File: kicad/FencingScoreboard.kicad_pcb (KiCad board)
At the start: 2 copper layers, 134.5 x 61 mm, 17 parts, among them IC1 PIC16F18855-I-ML, IC2 TLC59281RGE, IC3 TLC59281RGE, J1 USB_B_Micro, J2 Conn_01x04_Socket, Q1 2N7002

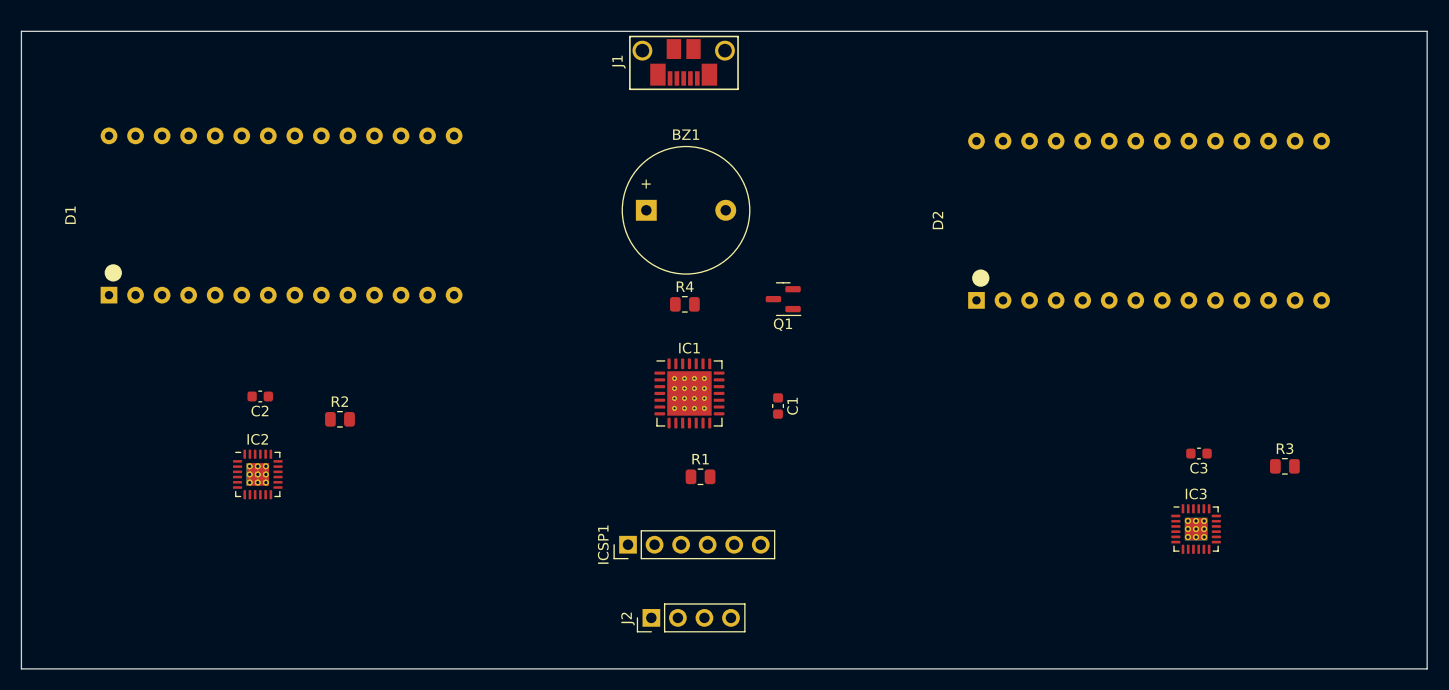
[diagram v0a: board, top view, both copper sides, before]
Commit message: Redesign for new LED driver, route PCB
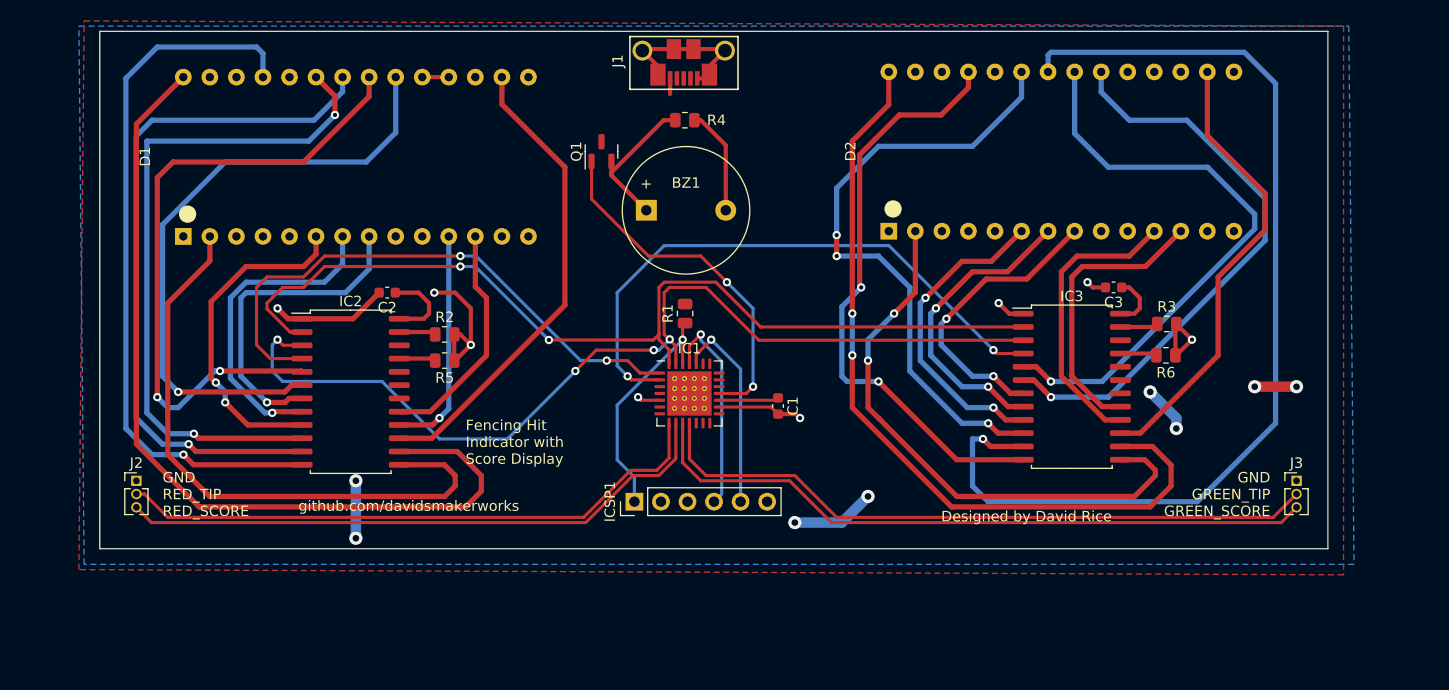
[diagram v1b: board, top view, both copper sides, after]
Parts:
- added J3: Conn_01x03_Pin, Connector_PinHeader_1.27mm:PinHeader_1x03_P1.27mm_Vertical, F.Cu at (204.0, 116.5)
- added R5: 10K, Resistor_SMD:R_0805_2012Metric, F.Cu at (122.5, 105.0)
- added R6: 10K, Resistor_SMD:R_0805_2012Metric, F.Cu at (191.5, 104.5)
- IC2, IC3: value TLC59281RGE -> STP16CPC26; footprint Package_DFN_QFN:QFN-24-1EP_4x4mm_P0.5mm_EP2.15x2.15mm_ThermalVias -> Package_SO:SOP-24_7.5x15.4mm_P1.27mm
- J2: value Conn_01x04_Socket -> Conn_01x03_Pin; footprint Connector_PinHeader_2.54mm:PinHeader_1x04_P2.54mm_Vertical -> Connector_PinHeader_1.27mm:PinHeader_1x03_P1.27mm_Vertical
- R2, R3: value 3K6 -> 2K
- moved J2 51.0 mm to (93.0, 116.5), turned to 0 degrees
- moved Q1 22.4 mm to (137.5, 85.0), turned to 90 degrees
- moved IC3 18.1 mm to (182.5, 107.5)
- moved C3 17.9 mm to (186.5, 98.0)
- moved R3 17.7 mm to (191.6, 101.5)
- moved R4 17.6 mm to (145.5, 82.0), turned to 180 degrees
- moved C2 15.7 mm to (117.0, 98.5)
- moved R1 15.7 mm to (145.5, 100.5), turned to 90 degrees
- moved R2 12.9 mm to (122.5, 102.5)
- moved IC2 11.9 mm to (113.5, 108.0)
- moved D2 10.7 mm to (165.0, 92.6)
- moved D1 9.06 mm to (97.5, 93.1)
- moved ICSP1 4.16 mm to (140.7, 118.5)
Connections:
- net Net-(IC1-ICSPCLK/RB6) renamed ICSPCLK
- net Net-(IC1-ISCPDAT/RB7) renamed ICSPDAT
- net Net-(IC1-RE3/~{MCLR}/VPP) renamed ~{MCLR}
- IC1 pad 10: Net-(IC1-RC2) -> GSC
- IC1 pad 11: Net-(IC1-RC3) -> GTIP
- IC1 pad 8: Net-(IC1-RC0) -> RTIP
- IC1 pad 9: Net-(IC1-RC1) -> RSC
- IC2 pad 1: Net-(IC1-RA2) -> GND
- IC2 pad 10: Net-(D1-D1D-) -> Net-(D1-D2F-)
- IC2 pad 11: Net-(D1-D1G-) -> Net-(D1-D2G-)
- IC2 pad 12: Net-(D1-D3A-) -> Net-(D1-D1A-)
- IC2 pad 13: Net-(D1-D3D-) -> Net-(D1-D1D-)
- IC2 pad 14: Net-(D1-D3G-) -> Net-(D1-D1G-)
- IC2 pad 15: unconnected-(IC2-OUT13-Pad15) -> Net-(D1-D3A-)
- IC2 pad 16: unconnected-(IC2-OUT14-Pad16) -> Net-(D1-D3D-)
- IC2 pad 17: unconnected-(IC2-OUT15-Pad17) -> Net-(D1-D3G-)
- IC2 pad 2: Net-(D1-D2A-) -> Net-(IC1-RA1)
- IC2 pad 20: Net-(IC2-IREF) -> unconnected-(IC2-OUT15-Pad20)
- IC2 pad 21: +5V -> Net-(IC2-~{OE})
- IC2 pad 22: GND -> unconnected-(IC2-SDO-Pad22)
- IC2 pad 23: Net-(IC1-RA1) -> Net-(IC2-R-EXT)
- IC2 pad 24: Net-(IC1-RA0) -> +5V
- IC2 pad 3: Net-(D1-D2B-) -> Net-(IC1-RA0)
- IC2 pad 4: Net-(D1-D2C-) -> Net-(IC1-RA2)
- IC2 pad 5: Net-(D1-D2D-) -> Net-(D1-D2A-)
- IC2 pad 6: Net-(D1-D2E-) -> Net-(D1-D2B-)
- IC2 pad 7: Net-(D1-D2F-) -> Net-(D1-D2C-)
- IC2 pad 8: Net-(D1-D2G-) -> Net-(D1-D2D-)
- IC2 pad 9: Net-(D1-D1A-) -> Net-(D1-D2E-)
- IC3 pad 1: Net-(IC1-RA3) -> GND
- IC3 pad 10: Net-(D2-D1D-) -> Net-(D2-D2F-)
- IC3 pad 11: Net-(D2-D1G-) -> Net-(D2-D2G-)
- IC3 pad 12: Net-(D2-D3A-) -> Net-(D2-D1A-)
- IC3 pad 13: Net-(D2-D3D-) -> Net-(D2-D1D-)
- IC3 pad 14: Net-(D2-D3G-) -> Net-(D2-D1G-)
- IC3 pad 15: unconnected-(IC3-OUT13-Pad15) -> Net-(D2-D3A-)
- IC3 pad 16: unconnected-(IC3-OUT14-Pad16) -> Net-(D2-D3D-)
- IC3 pad 17: unconnected-(IC3-OUT15-Pad17) -> Net-(D2-D3G-)
- IC3 pad 2: Net-(D2-D2A-) -> Net-(IC1-RA1)
- IC3 pad 20: Net-(IC3-IREF) -> unconnected-(IC3-OUT15-Pad20)
- IC3 pad 21: +5V -> Net-(IC3-~{OE})
- IC3 pad 22: GND -> unconnected-(IC3-SDO-Pad22)
- IC3 pad 23: Net-(IC1-RA1) -> Net-(IC3-R-EXT)
- IC3 pad 24: Net-(IC1-RA0) -> +5V
- IC3 pad 3: Net-(D2-D2B-) -> Net-(IC1-RA0)
- IC3 pad 4: Net-(D2-D2C-) -> Net-(IC1-RA3)
- IC3 pad 5: Net-(D2-D2D-) -> Net-(D2-D2A-)
- IC3 pad 6: Net-(D2-D2E-) -> Net-(D2-D2B-)
- IC3 pad 7: Net-(D2-D2F-) -> Net-(D2-D2C-)
- IC3 pad 8: Net-(D2-D2G-) -> Net-(D2-D2D-)
- IC3 pad 9: Net-(D2-D1A-) -> Net-(D2-D2E-)
- J2 pad 1: Net-(IC1-RC0) -> GND
- J2 pad 2: Net-(IC1-RC1) -> RTIP
- J2 pad 3: Net-(IC1-RC2) -> RSC
- R2 pad 1: Net-(IC2-IREF) -> Net-(IC2-R-EXT)
- R3 pad 1: Net-(IC3-IREF) -> Net-(IC3-R-EXT)
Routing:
- net Net-(D2-D2G-): track 0.00 -> 99.6 mm, vias 0 -> 1
- net Net-(IC1-RA0): track 0.00 -> 94.4 mm, vias 0 -> 4
- net Net-(IC1-RA1): track 0.00 -> 91.4 mm, vias 0 -> 2
- net Net-(D1-D1G-): track 0.00 -> 83.4 mm
- net GND: track 0.00 -> 77.3 mm, vias 0 -> 10
- net Net-(D2-D1G-): track 0.00 -> 76.4 mm, vias 0 -> 2
- net Net-(D1-D1A-): track 0.00 -> 68.7 mm, vias 0 -> 1
- net Net-(D1-D2G-): track 0.00 -> 67.0 mm, vias 0 -> 1
- net GSC: track 0.00 -> 65.5 mm
- net Net-(D1-D2F-): track 0.00 -> 65.3 mm, vias 0 -> 2
- net GTIP: track 0.00 -> 64.8 mm
- net Net-(D1-D2A-): track 0.00 -> 62.1 mm, vias 0 -> 2
- net Net-(D1-D2B-): track 0.00 -> 60.0 mm, vias 0 -> 1
- net Net-(D2-D2F-): track 0.00 -> 59.8 mm, vias 0 -> 3
- net Net-(D1-D1D-): track 0.00 -> 58.9 mm
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- added copper zone on F.Cu, net +5V
- added copper zone on B.Cu, net GND
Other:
- board size 134.5 x 61 mm -> 117.5 x 49.5 mm
- board text added: "Designed by David Rice"
- board text added: "Fencing Hit Indicator with Score Display"
- board text added: "GND GREEN_TIP GREEN_SCORE"
- board text added: "GND RED_TIP RED_SCORE"
- board text added: "github.com/davidsmakerworks"

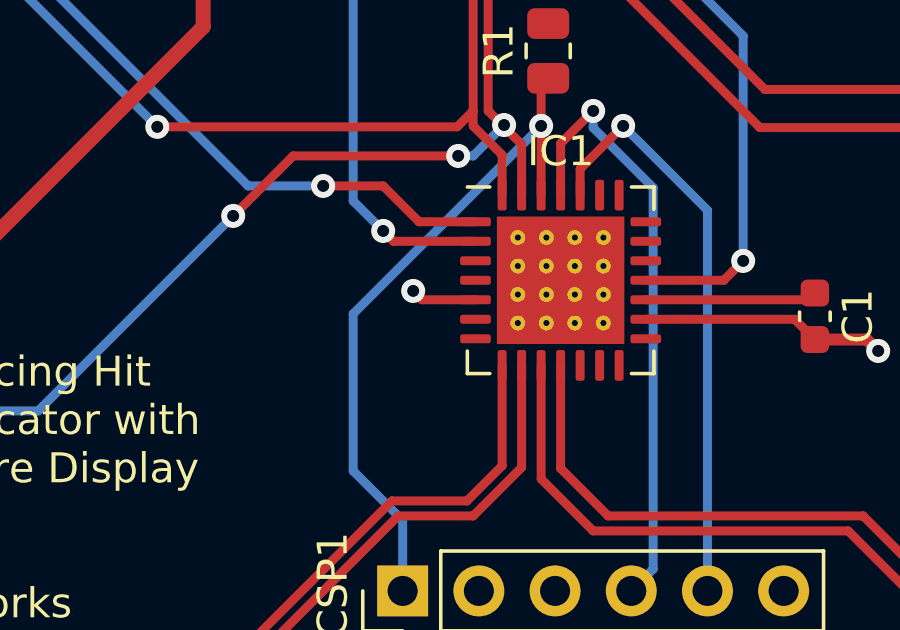
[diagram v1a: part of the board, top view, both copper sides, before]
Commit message: Update design rules, remove thermal vias
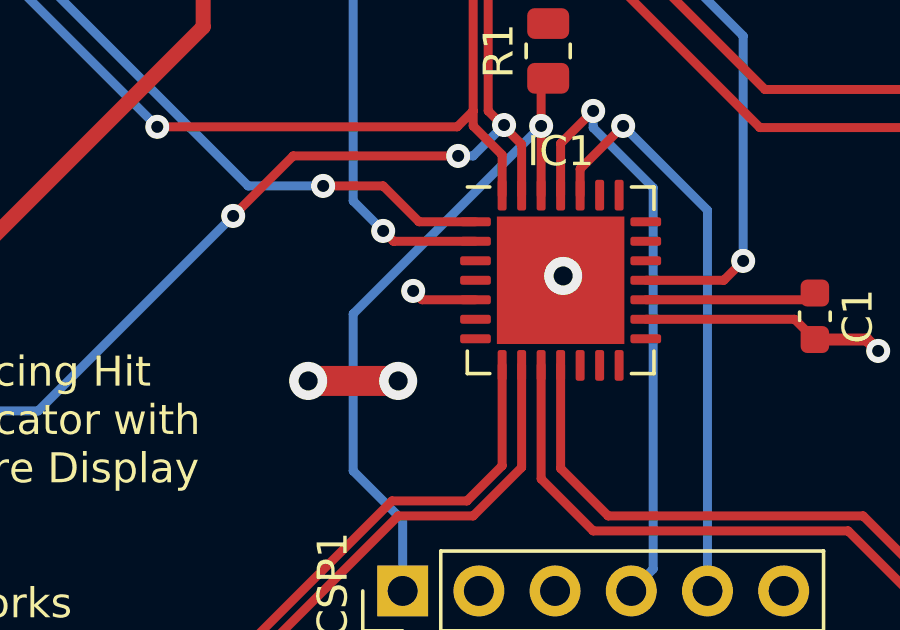
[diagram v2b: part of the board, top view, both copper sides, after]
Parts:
- IC1: footprint Package_DFN_QFN:QFN-28-1EP_6x6mm_P0.65mm_EP4.25x4.25mm_ThermalVias -> Package_DFN_QFN:QFN-28-1EP_6x6mm_P0.65mm_EP4.25x4.25mm
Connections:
- IC1 pad 29: (no net) -> GND
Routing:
- net GND: track 77.3 -> 80.5 mm, vias 10 -> 13

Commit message: Minor updates
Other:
- board text added: "GREEN"
- board text added: "RED"
- board text added: "USB_PWR"
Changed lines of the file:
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@@
     (property "ki_keywords" "cap capacitor")
     (attr smd)
-    (fp_text reference "C2" (at 0 -1.43) (layer "F.SilkS")
+    (fp_text reference "C2" (at 0 1.5) (layer "F.SilkS")
         (effects (font (size 1 1) (thickness 0.15)))
     )
@@
     (property "ki_keywords" "cap capacitor")
     (attr smd)
-    (fp_text reference "C3" (at 0 -1.43) (layer "F.SilkS")
+    (fp_text reference "C3" (at 0 1.5) (layer "F.SilkS")
         (effects (font (size 1 1) (thickness 0.15)))
     )
@@
     (property "ki_keywords" "connector")
     (attr through_hole)
-    (fp_text reference "ICSP1" (at 0 -2.33 90) (layer "F.SilkS")
+    (fp_text reference "ICSP1" (at -3 6.35 180) (layer "F.SilkS")
         (effects (font (size 1 1) (thickness 0.15)))
     )
@@
     (effects (font (size 1 1) (thickness 0.15)) (justify left bottom))
   )
-  (gr_text "Designed by David Rice" (at 170 120.5) (layer "F.SilkS")
+  (gr_text "GREEN" (at 170 88) (layer "F.SilkS")
+    (effects (font (size 5 5) (thickness 0.4)) (justify left bottom))
+  )
+  (gr_text "Designed by David Rice" (at 168 119) (layer "F.SilkS")
     (effects (font (size 1 1) (thickness 0.15)) (justify left bottom))
   )
-  (gr_text "Fencing Hit\nIndicator with\nScore Display" (at 124.5 115) (layer "F.SilkS")
+  (gr_text "RED" (at 106 89) (layer "F.SilkS")
+    (effects (font (size 5 5) (thickness 0.4)) (justify left bottom))
+  )
+  (gr_text "Fencing Hit\nIndicator with\nScore Display" (at 126 113.5) (layer "F.SilkS")
     (effects (font (size 1 1) (thickness 0.15)) (justify left bottom))
   )
-  (gr_text "github.com/davidsmakerworks" (at 108.5 119.5) (layer "F.SilkS")
+  (gr_text "github.com/davidsmakerworks" (at 166 121) (layer "F.SilkS")
     (effects (font (size 1 1) (thickness 0.15)) (justify left bottom))
   )
@@
     (effects (font (size 1 1) (thickness 0.15)) (justify right bottom))
   )
+  (gr_text "USB_PWR" (at 152 76.5) (layer "F.SilkS")
+    (effects (font (size 1 1) (thickness 0.15)) (justify left bottom))
+  )
   (segment (start 138.45 87) (end 138.45 87.28) (width 0.4) (layer "F.Cu") (net 1))

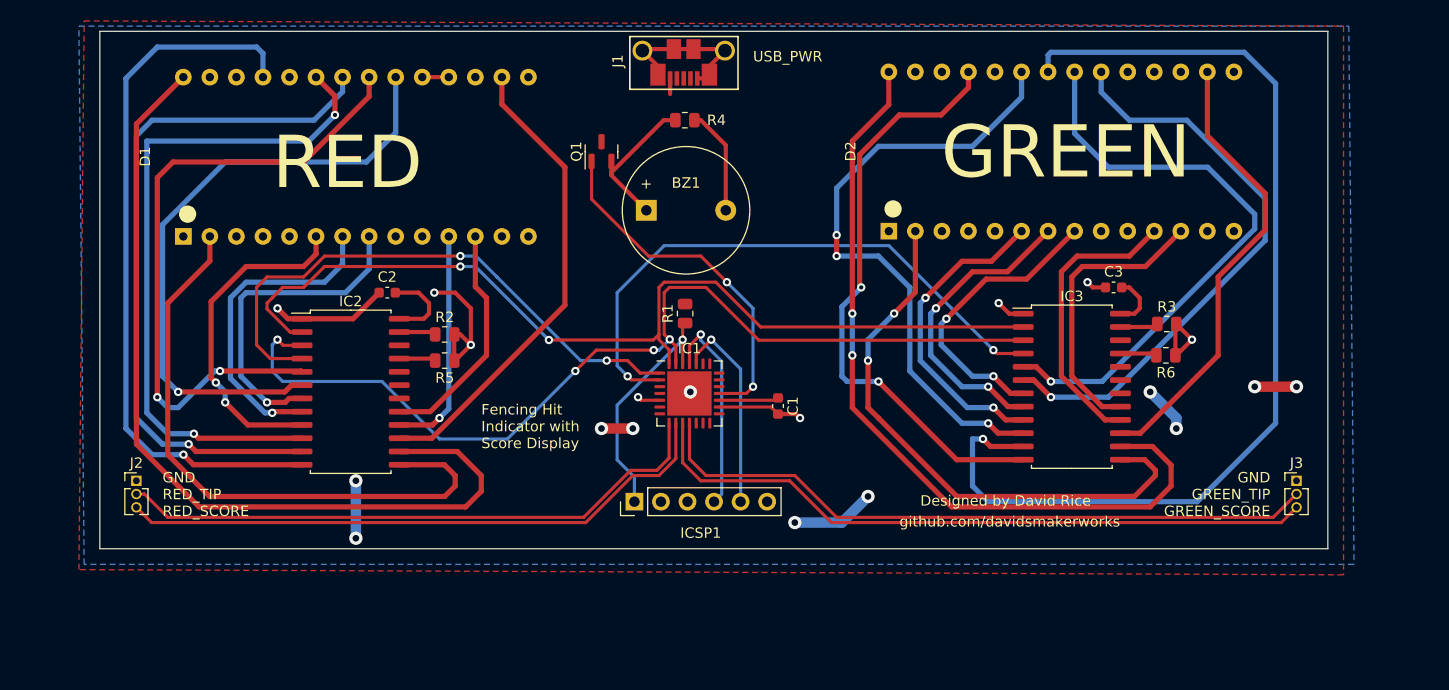
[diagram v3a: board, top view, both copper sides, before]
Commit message: Schematic cleanup, start PCB re-route
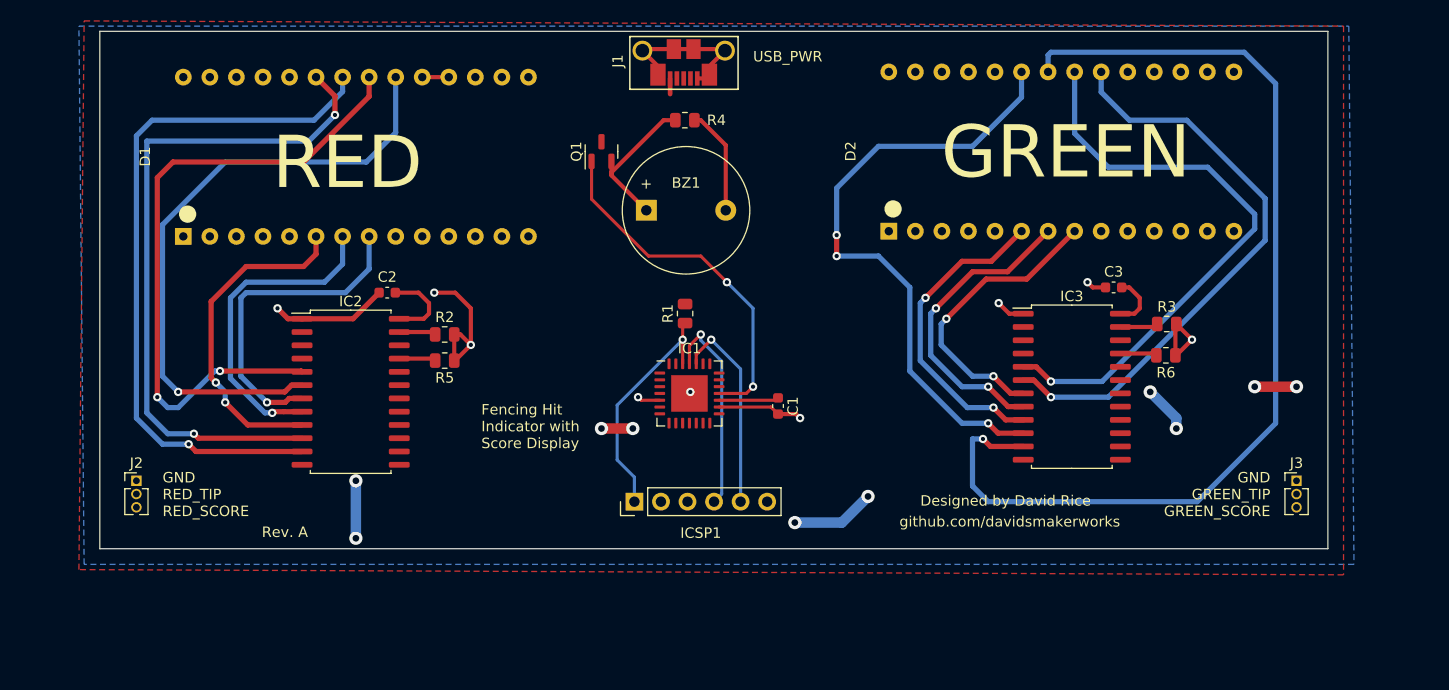
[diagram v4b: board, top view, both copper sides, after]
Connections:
- net Net-(D1-D2A-) renamed R_OUT0
- net Net-(D1-D2B-) renamed R_OUT1
- net Net-(D1-D2C-) renamed R_OUT2
- net Net-(D1-D2D-) renamed R_OUT3
- net Net-(D1-D2E-) renamed R_OUT4
- net Net-(D1-D2F-) renamed R_OUT5
- net Net-(D1-D2G-) renamed R_OUT6
- net Net-(D2-D2A-) renamed G_OUT0
- net Net-(D2-D2B-) renamed G_OUT1
- net Net-(D2-D2C-) renamed G_OUT2
- net Net-(D2-D2D-) renamed G_OUT3
- net Net-(D2-D2E-) renamed G_OUT4
- net Net-(D2-D2F-) renamed G_OUT5
- net Net-(D2-D2G-) renamed G_OUT6
- net Net-(IC1-RB0) renamed BZ_PWM
- D1 pad 11: Net-(D1-D3D-) -> R_OUT12
- D1 pad 12: Net-(D1-D3G-) -> R_OUT13
- D1 pad 16: Net-(D1-D3A-) -> R_OUT11
- D1 pad 2: Net-(D1-D1D-) -> R_OUT9
- D1 pad 25: Net-(D1-D1A-) -> R_OUT8
- D1 pad 28: Net-(D1-D1G-) -> R_OUT10
- D2 pad 11: Net-(D2-D3D-) -> G_OUT12
- D2 pad 12: Net-(D2-D3G-) -> G_OUT13
- D2 pad 16: Net-(D2-D3A-) -> G_OUT11
- D2 pad 2: Net-(D2-D1D-) -> G_OUT9
- D2 pad 25: Net-(D2-D1A-) -> G_OUT8
- D2 pad 28: Net-(D2-D1G-) -> G_OUT10
- IC1 pad 1: Net-(IC1-RA2) -> GSC
- IC1 pad 10: GSC -> RED_LE
- IC1 pad 11: GTIP -> GRN_LE
- IC1 pad 2: Net-(IC1-RA3) -> GTIP
- IC1 pad 27: Net-(IC1-RA0) -> RTIP
- IC1 pad 28: Net-(IC1-RA1) -> RSC
- IC1 pad 8: RTIP -> LED_CLK
- IC1 pad 9: RSC -> LED_DAT
- IC2 pad 12: Net-(D1-D1A-) -> unconnected-(IC2-OUT7-Pad12)
- IC2 pad 13: Net-(D1-D1D-) -> R_OUT8
- IC2 pad 14: Net-(D1-D1G-) -> R_OUT9
- IC2 pad 15: Net-(D1-D3A-) -> R_OUT10
- IC2 pad 16: Net-(D1-D3D-) -> R_OUT11
- IC2 pad 17: Net-(D1-D3G-) -> R_OUT12
- IC2 pad 18: unconnected-(IC2-OUT13-Pad18) -> R_OUT13
- IC2 pad 2: Net-(IC1-RA1) -> LED_DAT
- IC2 pad 3: Net-(IC1-RA0) -> LED_CLK
- IC2 pad 4: Net-(IC1-RA2) -> RED_LE
- IC3 pad 12: Net-(D2-D1A-) -> unconnected-(IC3-OUT7-Pad12)
- IC3 pad 13: Net-(D2-D1D-) -> G_OUT8
- IC3 pad 14: Net-(D2-D1G-) -> G_OUT9
- IC3 pad 15: Net-(D2-D3A-) -> G_OUT10
- IC3 pad 16: Net-(D2-D3D-) -> G_OUT11
- IC3 pad 17: Net-(D2-D3G-) -> G_OUT12
- IC3 pad 18: unconnected-(IC3-OUT13-Pad18) -> G_OUT13
- IC3 pad 2: Net-(IC1-RA1) -> LED_DAT
- IC3 pad 3: Net-(IC1-RA0) -> LED_CLK
- IC3 pad 4: Net-(IC1-RA3) -> GRN_LE
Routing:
- net Net-(IC1-RA0): track 94.4 -> 0.00 mm, vias 4 -> 0
- net Net-(IC1-RA1): track 91.4 -> 0.00 mm, vias 2 -> 0
- net Net-(D1-D1G-): track 83.4 -> 0.00 mm
- net Net-(D2-D1G-): track 76.4 -> 0.00 mm, vias 2 -> 0
- net Net-(D1-D1A-): track 68.7 -> 0.00 mm, vias 1 -> 0
- net GSC: track 65.5 -> 0.00 mm
- net GTIP: track 64.8 -> 0.00 mm
- net Net-(D1-D1D-): track 58.9 -> 0.00 mm
- net RSC: track 58.2 -> 0.00 mm
- net RTIP: track 57.6 -> 0.00 mm
- net Net-(D2-D1A-): track 57.2 -> 0.00 mm, vias 2 -> 0
- net Net-(IC1-RA3): track 56.6 -> 0.00 mm, vias 2 -> 0
- net Net-(D2-D1D-): track 54.9 -> 0.00 mm, vias 2 -> 0
- net Net-(IC1-RA2): track 54.8 -> 0.00 mm, vias 2 -> 0
- net Net-(D1-D3A-): track 45.4 -> 0.00 mm
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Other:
- board text added: "Rev. A"
